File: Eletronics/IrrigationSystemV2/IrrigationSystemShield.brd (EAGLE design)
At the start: 102.5 x 58.4 mm, 51 parts, among them T1-THERM2 THERMISTOR-2,5, U1 ARDUINO-MEGANOSILK, U1-SOL1 RELAY-SOLIDSTATEPTH, U1-SOL2 RELAY-SOLIDSTATEPTH

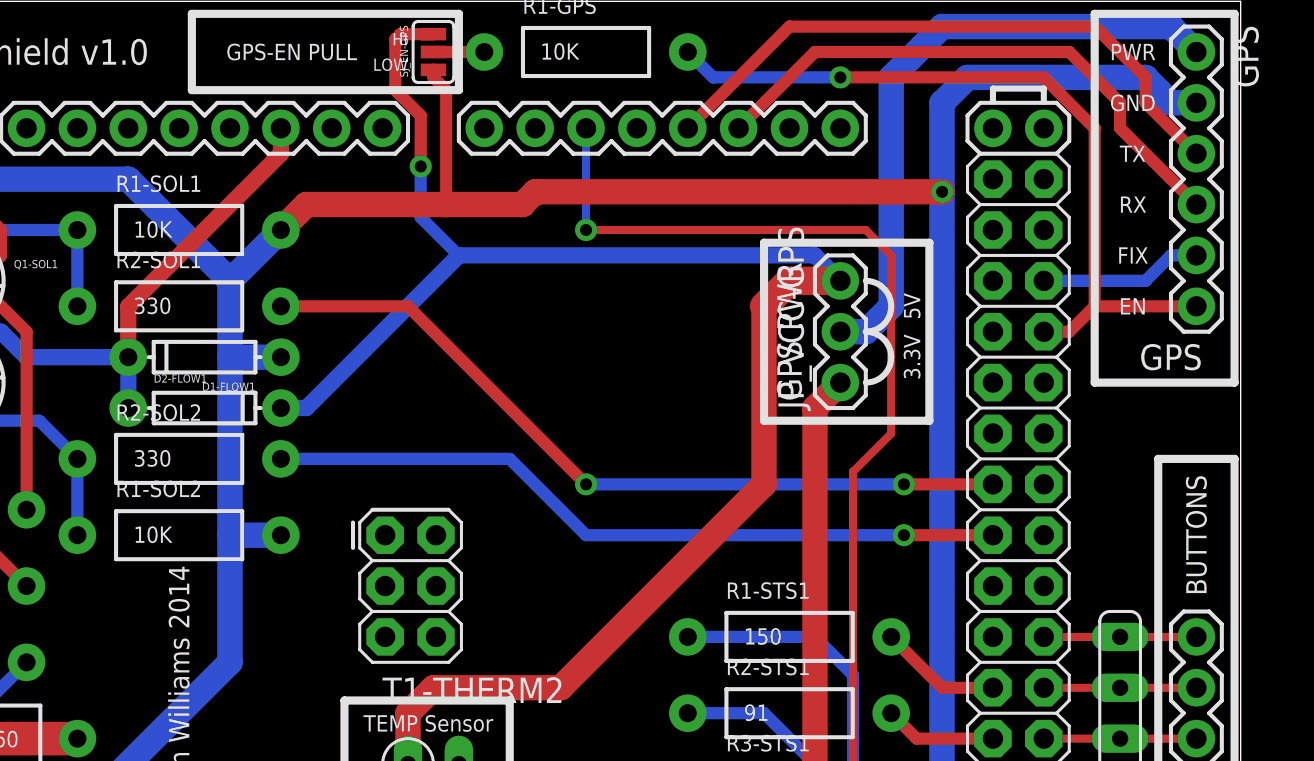
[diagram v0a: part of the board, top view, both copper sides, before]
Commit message: Added ability to add Interrupt to PB5.
Updated Schematic to include interrupt. Need to run trace for
interrupt. If trace is not run PB5 will still work as a non interrupted
pin.
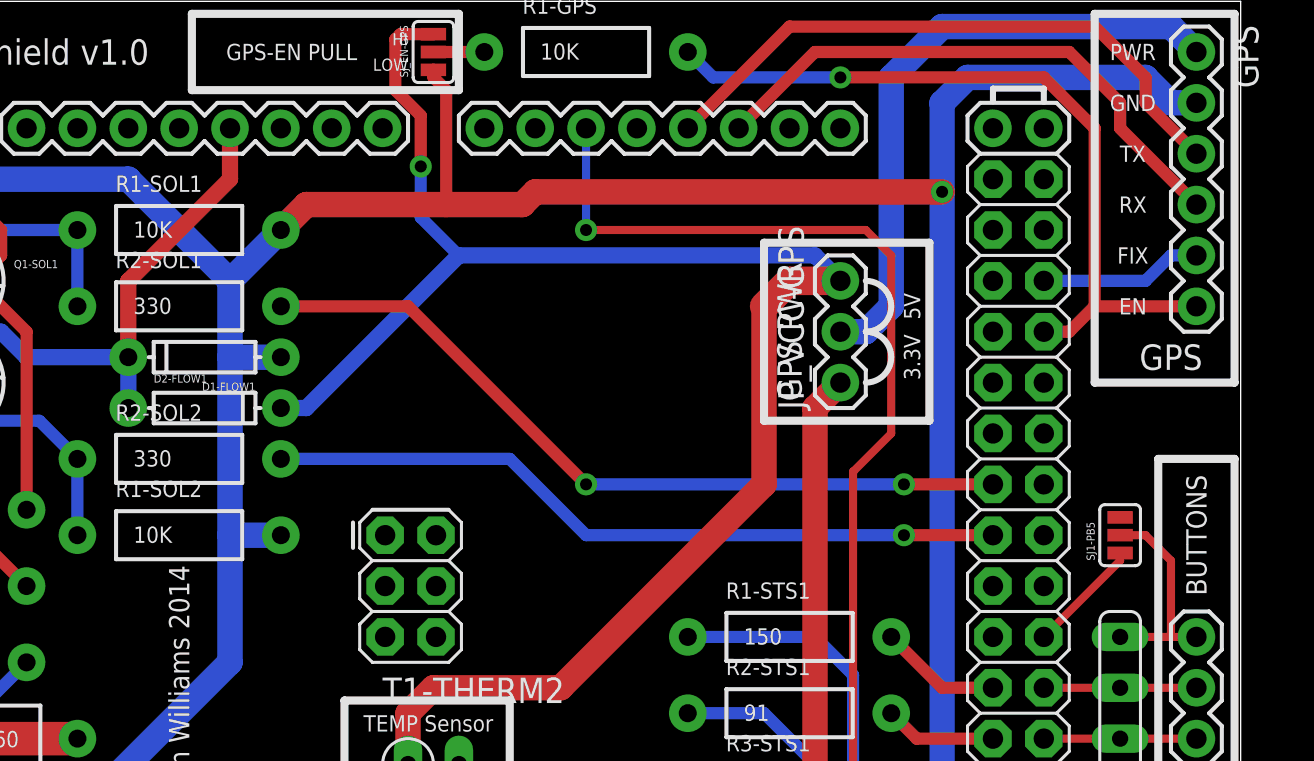
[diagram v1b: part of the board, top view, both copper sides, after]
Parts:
- added SJ1-PB5: (no value), SparkFun-Passives:SJ_3
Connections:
- new net PB5I: SJ1-PB5.3, U1.2
- new net PB5RAW: BUTTONS.7, RN1.7, SJ1-PB5.2
- net FLOW1: now also U1.3; no longer U1.2
- net PB5: now also SJ1-PB5.1; no longer BUTTONS.7, RN1.7
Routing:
- net PB5RAW: track 0.00 -> 10.7 mm
- net PB5: track 7.62 -> 5.77 mm
- net FLOW1: track 58.2 -> 57.2 mm
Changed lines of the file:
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@@
 <attribute name="PROD_ID" value="DIO-09434" x="83.82" y="13.97" size="1.778" layer="27" display="off"/>
 </element>
+<element name="SJ1-PB5" library="SparkFun-Passives" package="SJ_3" value="" x="96.52" y="31.75" rot="R90"/>
 </elements>
 <signals>
@@
 <wire x1="16.47" y1="52.07" x2="16.47" y2="54.57" width="0.8128" layer="16"/>
 <wire x1="16.47" y1="54.57" x2="17.78" y2="55.88" width="0.8128" layer="16"/>
-<contactref element="U1" pad="2"/>
-<wire x1="46.99" y1="40.64" x2="46.99" y2="43.18" width="0.8128" layer="1"/>
-<wire x1="46.99" y1="43.18" x2="54.61" y2="50.8" width="0.8128" layer="1"/>
-<wire x1="54.61" y1="50.8" x2="54.61" y2="52.07" width="0.8128" layer="1"/>
+<contactref element="U1" pad="3"/>
+<wire x1="46.99" y1="40.64" x2="46.99" y2="44.45" width="0.8128" layer="1"/>
+<wire x1="46.99" y1="44.45" x2="52.07" y2="49.53" width="0.8128" layer="1"/>
+<wire x1="52.07" y1="49.53" x2="52.07" y2="52.07" width="0.8128" layer="1"/>
 </signal>
 <signal name="SIG-FLOW1">
@@
 </signal>
 <signal name="PB5">
-<contactref element="BUTTONS" pad="7"/>
-<contactref element="RN1" pad="7"/>
 <contactref element="U1" pad="41"/>
-<wire x1="100.33" y1="26.67" x2="96.52" y2="26.67" width="0.4064" layer="1"/>
-<wire x1="96.52" y1="26.67" x2="92.71" y2="26.67" width="0.4064" layer="1"/>
+<contactref element="SJ1-PB5" pad="1"/>
+<wire x1="96.52" y1="30.861" x2="96.52" y2="30.48" width="0.4064" layer="1"/>
+<wire x1="96.52" y1="30.48" x2="92.71" y2="26.67" width="0.4064" layer="1"/>
 </signal>
 <signal name="PB4">
@@
 <wire x1="90.17" y1="19.05" x2="85.09" y2="19.05" width="0.6096" layer="1"/>
 </signal>
+<signal name="PB5RAW">
+<contactref element="BUTTONS" pad="7"/>
+<contactref element="RN1" pad="7"/>
+<wire x1="100.33" y1="26.67" x2="99.06" y2="26.67" width="0.4064" layer="1"/>
+<contactref element="SJ1-PB5" pad="2"/>
+<wire x1="99.06" y1="26.67" x2="96.52" y2="26.67" width="0.4064" layer="1"/>
+<wire x1="96.52" y1="31.75" x2="97.79" y2="31.75" width="0.4064" layer="1"/>
+<wire x1="97.79" y1="31.75" x2="99.06" y2="30.48" width="0.4064" layer="1"/>
+<wire x1="99.06" y1="30.48" x2="99.06" y2="26.67" width="0.4064" layer="1"/>
+</signal>
+<signal name="PB5I">
+<contactref element="SJ1-PB5" pad="3"/>
+<contactref element="U1" pad="2"/>
+<wire x1="96.52" y1="32.639" x2="54.61" y2="52.07" width="0" layer="19" extent="1-1"/>
+</signal>
 </signals>
